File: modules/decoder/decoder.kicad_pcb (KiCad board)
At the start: 2 copper layers, 107.5 x 140 mm, 27 parts, among them J10 Conn_02x05_Odd_Even, J13 Conn_02x04_Odd_Even, J16 Conn_01x04, K1 4PDT, K2 4PDT, K3 4PDT, K4 4PDT, K5 4PDT, K6 4PDT

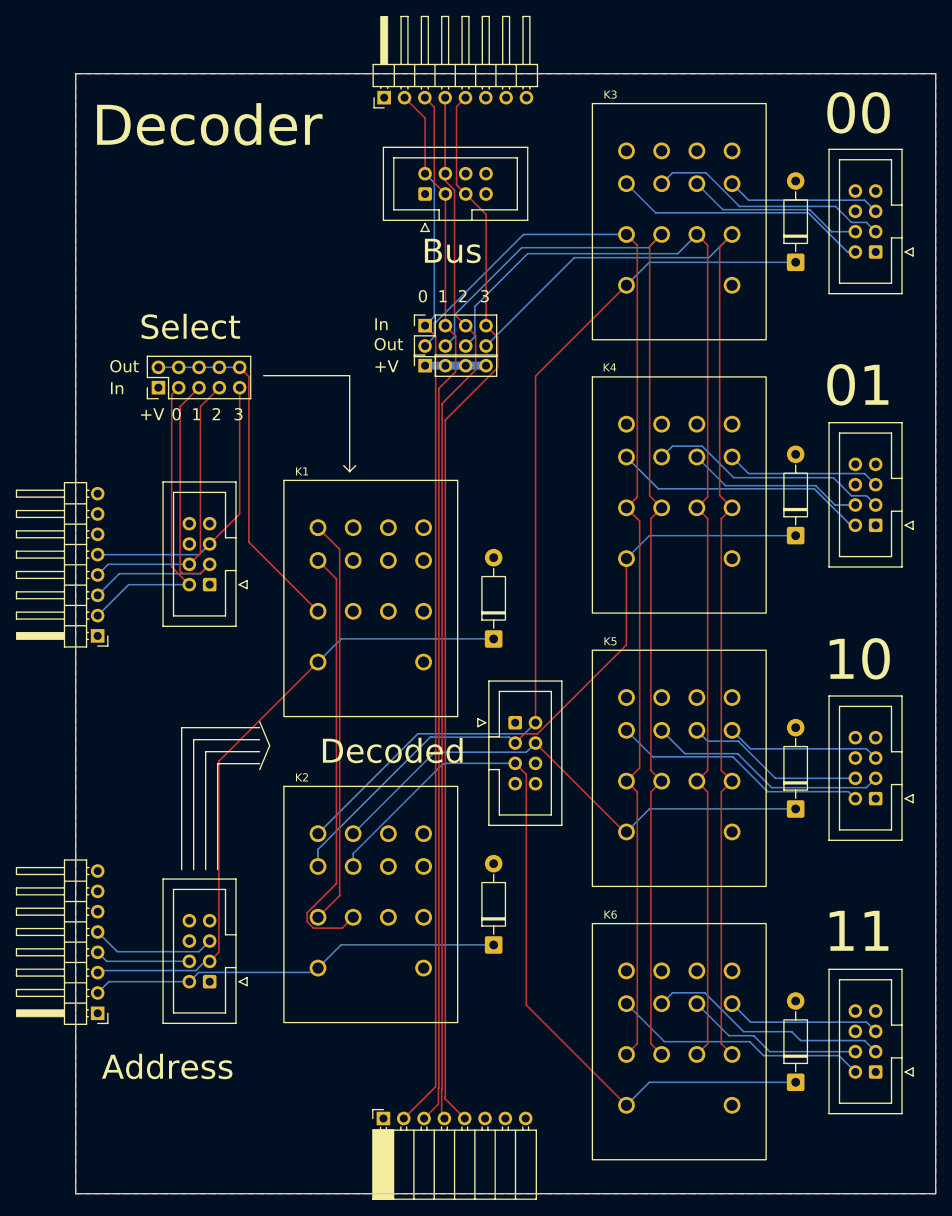
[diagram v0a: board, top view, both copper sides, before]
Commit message: Added switchboard module
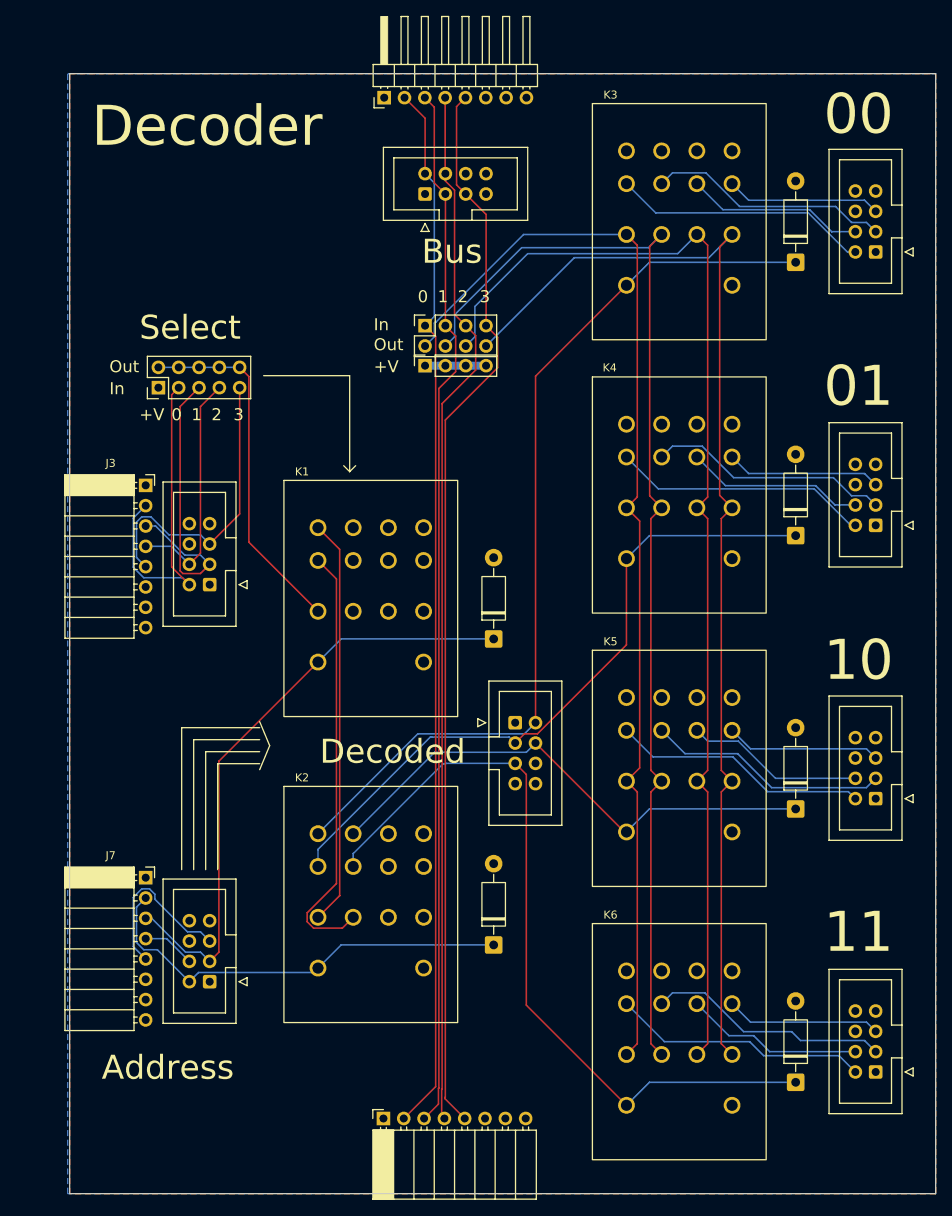
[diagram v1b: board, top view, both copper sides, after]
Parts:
- J3, J7: footprint Connector_PinHeader_2.54mm:PinHeader_1x08_P2.54mm_Horizontal -> Connector_PinSocket_2.54mm:PinSocket_1x08_P2.54mm_Horizontal
- moved J3 19.8 mm to (60.8, 87.5), turned to 0 degrees
- moved J7 18.0 mm to (60.8, 136.5), turned to 0 degrees
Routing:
- net Net-(J1-D3): track 15.6 -> 21.4 mm
- net Net-(J10-Pin_5): track 43.8 -> 38.2 mm
- net Net-(J10-Pin_7): track 35.6 -> 30.0 mm
- net Net-(J1-D2): track 11.9 -> 6.64 mm
- net Net-(D1-K): track 80.8 -> 77.0 mm
- net Net-(J10-Pin_3): track 39.0 -> 42.2 mm
- net Net-(D2-K): track 52.0 -> 54.6 mm
- net Net-(J10-Pin_9): track 35.6 -> 38.0 mm
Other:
- board size 107.5 x 140 mm -> 108.2 x 140 mm

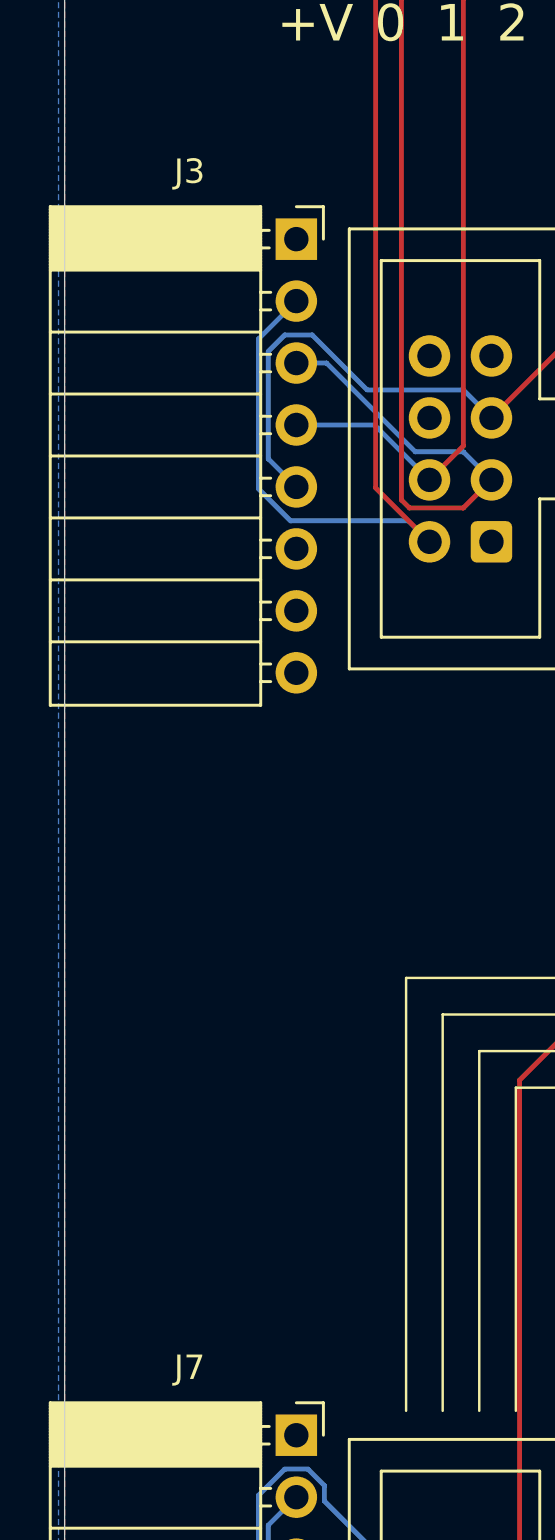
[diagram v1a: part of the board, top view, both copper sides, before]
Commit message: Added new switchboard
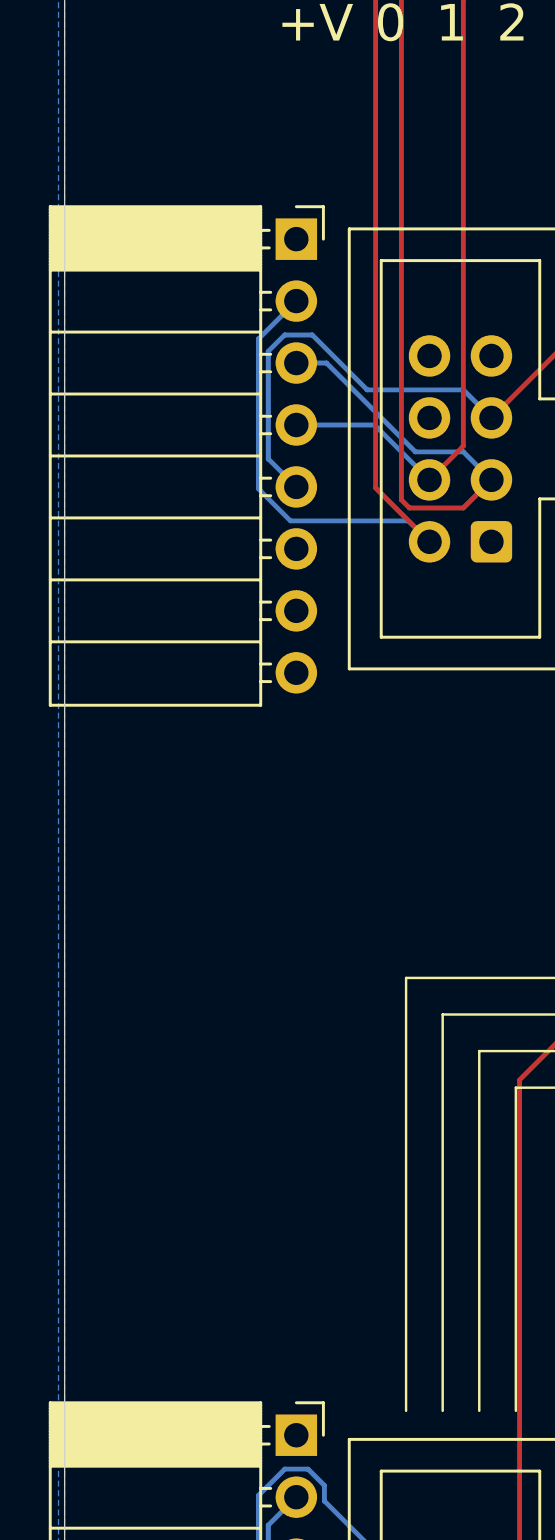
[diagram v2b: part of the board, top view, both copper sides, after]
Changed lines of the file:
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@@
 			(at -4.38 -2.77 0)
 			(layer "F.SilkS")
+			(hide yes)
 			(effects
 				(font
@@
 			(at -4.38 20.55 0)
 			(layer "F.Fab")
+			(hide yes)
 			(effects
 				(font
@@
 			)
 			(layer "F.Fab")
-		)
-		(fp_text user "${REFERENCE}"
-			(at -5.775 8.89 90)
-			(layer "F.Fab")
-			(effects
-				(font
-					(size 1 1)
-					(thickness 0.15)
-				)
-			)
 		)
 		(pad "1" thru_hole rect
@@
 			(at -4.38 -2.77 0)
 			(layer "F.SilkS")
+			(hide yes)
 			(effects
 				(font
@@
 			(at -4.38 20.55 0)
 			(layer "F.Fab")
+			(hide yes)
 			(effects
 				(font
@@
 			(layer "F.Fab")
 		)
-		(fp_text user "${REFERENCE}"
-			(at -5.775 8.89 90)
-			(layer "F.Fab")
-			(effects
-				(font
-					(size 1 1)
-					(thickness 0.15)
-				)
-			)
-		)
 		(pad "1" thru_hole rect
